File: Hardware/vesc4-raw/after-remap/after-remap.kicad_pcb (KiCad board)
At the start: 4 copper layers, 40.3 x 65 mm, 129 parts, among them K1 SERVO, P1 HALL/Encoder, P101 CANBUS, P2 SWD, P3 PWR_COMM, P4 IN+, P5 IN-, P6 MOTOR1, P7 MOTOR2, P9 MOTOR3, Q1 IPT007N06NATMA1, Q2 IPT007N06NATMA1, Q3 IPT007N06NATMA1, Q4 IPT007N06NATMA1, Q5 IPT007N06NATMA1, Q6 IPT007N06NATMA1, U1 STM32F40X_LQFP64, U2 TC2117, U3 DRV8302, U401 SN65HVD232, X2 8MHz 10ppm

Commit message: pindahin d6
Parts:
- moved D6 25.8 mm to (78.4, 135.5), turned to 90 degrees
- moved C2 0.66 mm to (83.7, 127.1)
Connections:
- net Net-(U4-D+) renamed /D+
- net Net-(U4-D-) renamed /D-
- U4 pad 1: Net-(USB1-VCC) -> Net-(D6-A)
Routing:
- net /D+: track 4.28 -> 6.64 mm
- net /D-: track 3.97 -> 6.16 mm
- net /MCU/AN_IN: track 28.9 -> 27.4 mm

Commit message: usb kelar trace
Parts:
- D4: moved to B.Cu
- moved D4 14.3 mm to (74.0, 120.7), turned to 180 degrees
- moved 1PIN 1.90 mm to (79.6, 142.0)
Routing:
- net GND: track 387.3 -> 395.4 mm
- net Net-(D6-A): track 0.00 -> 5.66 mm
- net +5V: track 115.3 -> 119.3 mm

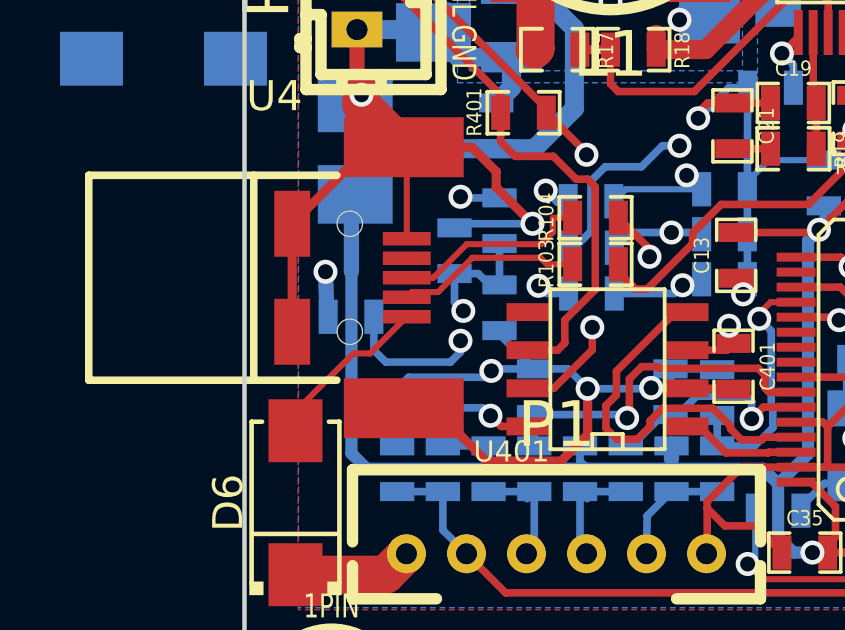
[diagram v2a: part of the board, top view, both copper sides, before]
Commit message: hapus r6 0r sama via
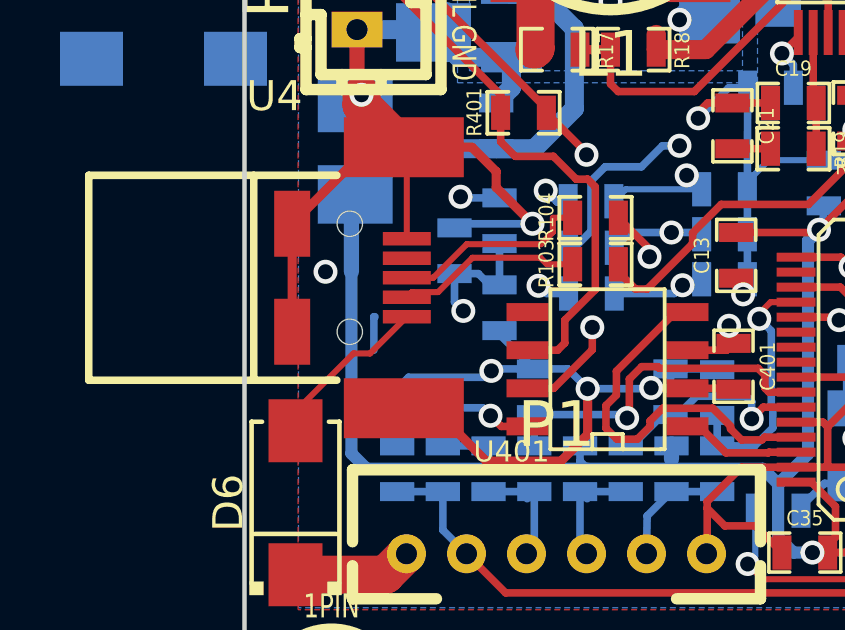
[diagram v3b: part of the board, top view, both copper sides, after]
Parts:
- removed R6: 0R, CRF1:SMD-0603_r
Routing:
- net Net-(USB1-VCC): track 4.72 -> 1.15 mm, vias 1 -> 0
- net +5V: track 119.3 -> 117.8 mm
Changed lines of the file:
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@@
 	(footprint "CRF1:SMD-0603_r"
 		(layer "B.Cu")
-		(at 80.25 129.3 180)
-		(property "Reference" "R6"
-			(at 1.635 -0.024 90)
-			(layer "B.SilkS")
-			(effects
-				(font
-					(size 0.50038 0.4572)
-					(thickness 0.1143)
-				)
-				(justify mirror)
-			)
-		)
-		(property "Value" "0R"
-			(at -1.69926 0 90)
-			(layer "B.SilkS")
-			(hide yes)
-			(effects
-				(font
-					(size 0.508 0.4572)
-					(thickness 0.1143)
-				)
-				(justify mirror)
-			)
-		)
-		(property "Datasheet" ""
-			(at 0 0 0)
-			(layer "B.Fab")
-			(hide yes)
-			(effects
-				(font
-					(size 1.27 1.27)
-					(thickness 0.15)
-				)
-				(justify mirror)
-			)
-		)
-		(property "Description" ""
-			(at 0 0 0)
-			(layer "B.Fab")
-			(hide yes)
-			(effects
-				(font
-					(size 1.27 1.27)
-					(thickness 0.15)
-				)
-				(justify mirror)
-			)
-		)
-		(property ki_fp_filters "R? SM0603 SM0805 R?-* SM1206")
-		(sheetname "/")
-		(sheetfile "after-remap.kicad_sch")
-		(attr smd)
-		(fp_line
-			(start 1.2065 0.6985)
-			(end 1.2065 -0.6985)
-			(stroke
-				(width 0.127)
-				(type solid)
-			)
-			(layer "B.SilkS")
-		)
-		(fp_line
-			(start 1.2065 0.6985)
-			(end 0.50038 0.6985)
-			(stroke
-				(width 0.127)
-				(type solid)
-			)
-			(layer "B.SilkS")
-		)
-		(fp_line
-			(start 1.2065 -0.6985)
-			(end 0.50038 -0.6985)
-			(stroke
-				(width 0.127)
-				(type solid)
-			)
-			(layer "B.SilkS")
-		)
-		(fp_line
-			(start -0.50038 0.6985)
-			(end -1.2065 0.6985)
-			(stroke
-				(width 0.127)
-				(type solid)
-			)
-			(layer "B.SilkS")
-		)
-		(fp_line
-			(start -1.2065 0.6985)
-			(end -1.2065 -0.6985)
-			(stroke
-				(width 0.127)
-				(type solid)
-			)
-			(layer "B.SilkS")
-		)
-		(fp_line
-			(start -1.2065 -0.6985)
-			(end -0.50038 -0.6985)
-			(stroke
-				(width 0.127)
-				(type solid)
-			)
-			(layer "B.SilkS")
-		)
-		(pad "1" smd rect
-			(at -0.762 0 180)
-			(size 0.635 1.143)
-			(layers "B.Cu" "B.Mask" "B.Paste")
-			(net 114 "Net-(USB1-VCC)")
-			(pintype "passive")
-		)
-		(pad "2" smd rect
-			(at 0.762 0 180)
-			(size 0.635 1.143)
-			(layers "B.Cu" "B.Mask" "B.Paste")
-			(net 1 "+5V")
-			(pintype "passive")
-		)
-		(embedded_fonts no)
-		(model "smd\\resistors\\R0603.wrl"
-			(offset
-				(xyz 0 0 0.02540000082)
-			)
-			(scale
-				(xyz 0.5 0.5 0.5)
-			)
-			(rotate
-				(xyz 0 0 0)
-			)
-		)
-	)
-	(footprint "CRF1:SMD-0603_r"
-		(layer "B.Cu")
 		(at 83.312 134.366 90)
 		(property "Reference" "R7"
@@
 	)
 	(segment
-		(start 79.45 129.262)
-		(end 79.4 127.8)
-		(width 0.508)
-		(layer "B.Cu")
-		(net 1)
-	)
-	(segment
 		(start 83.698 116.078)
 		(end 83 116.776)
@@
 	)
 	(segment
-		(start 79.488 129.3)
-		(end 79.45 129.262)
-		(width 0.508)
-		(layer "B.Cu")
-		(net 1)
-	)
-	(segment
 		(start 108.63326 133.096)
 		(end 108.63326 133.27126)
@@
 		(net 96)
 	)
-	(via
-		(at 83.9 130.1)
-		(size 0.8)
-		(drill 0.5)
-		(layers "F.Cu" "B.Cu")
-		(net 114)
-	)
 	(segment
 		(start 81.05 129.3)
@@
 	)
 	(segment
-		(start 83.9 130.476)
-		(end 83.566 130.81)
-		(width 0.254)
-		(layer "B.Cu")
-		(net 114)
-	)
-	(segment
-		(start 83.566 130.81)
-		(end 81.407 130.81)
-		(width 0.254)
-		(layer "B.Cu")
-		(net 114)
-	)
-	(segment
-		(start 81.407 130.81)
-		(end 81.012 130.415)
-		(width 0.254)
-		(layer "B.Cu")
-		(net 114)
-	)
-	(segment
 		(start 81.012 130.415)
 		(end 81.012 129.3)
 		(width 0.254)
 		(layer "B.Cu")
-		(net 114)
-	)
-	(segment
-		(start 83.9 130.1)
-		(end 83.9 130.476)
-		(width 0.254)
-		(layer "B.Cu")

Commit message: sebelum pasang d4
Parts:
- moved D4 2.04 mm to (72.0, 120.3)
- moved C25 0.98 mm to (79.5, 124.1), turned to 0 degrees
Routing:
- net GND: track 395.4 -> 399.5 mm
- net +5V: track 117.8 -> 115.8 mm, vias 4 -> 3
- net VCC: track 185.3 -> 186.6 mm

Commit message: habis pasang d4
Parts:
- removed the D4 at (87.0, 113.0)
- moved D4 16.7 mm to (87.0, 113.0)
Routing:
- net GND: track 399.5 -> 396.9 mm
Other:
- board text added: "SEM"

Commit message: cp
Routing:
- net /Power MOSFETS/Q2-g: track 18.6 -> 17.3 mm
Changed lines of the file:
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@@
-	)
-	(segment
-		(start 104.394 95.377)
-		(end 104.871 94.9)
-		(width 0.2032)
-		(layer "B.Cu")
-		(net 86)
 	)
 	(segment
@@
 	)
 	(segment
-		(start 105.5939 94.9029)
-		(end 114.4029 94.9029)
+		(start 105.7419 96.7249)
+		(end 114.6902 96.7249)
 		(width 0.2032)
 		(layer "B.Cu")
@@
 	)
 	(segment
-		(start 104.871 94.9)
-		(end 105.5939 94.9)
+		(start 104.394 95.377)
+		(end 105.7419 96.7249)
+		(width 0.2032)
+		(layer "B.Cu")
+		(net 86)
+	)
+	(segment
+		(start 114.6902 96.7249)
+		(end 114.8 96.8347)
+		(width 0.2032)
+		(layer "B.Cu")
+		(net 86)
+	)
+	(segment
+		(start 114.8 96.8347)
+		(end 114.8 98.6)
 		(width 0.2032)
 		(layer "B.Cu")
@@
 		(width 0.2032)
 		(layer "B.Cu")
-		(net 86)
-	)
-	(segment
-		(start 105.5939 94.9)
-		(end 105.5939 94.9029)
-		(width 0.2032)
-		(layer "B.Cu")
-		(net 86)
-	)
-	(segment
-		(start 114.8 95.3)
-		(end 114.8 98.6)
-		(width 0.2032)
-		(layer "B.Cu")
-		(net 86)
-	)
-	(segment
-		(start 114.4029 94.9029)
-		(end 114.8 95.3)
-		(width 0.2032)
-		(layer "B.Cu")

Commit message: checkpoint
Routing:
- net Net-(USB1-VCC): track 1.15 -> 0.00 mm
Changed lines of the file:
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@@
 		(tenting front back)
 		(pcbplotparams
-			(layerselection 0x00000000_00000000_00000000_0200a0ff)
+			(layerselection 0x00000000_00000000_55555555_5755f5ff)
 			(plot_on_all_layers_selection 0x00000000_00000000_00000000_00000000)
 			(disableapertmacros no)
@@
 	(net 112 "unconnected-(U3-PWRGD-Pad4)")
 	(net 113 "unconnected-(U401-Vref-Pad5)")
-	(net 114 "Net-(USB1-VCC)")
-	(net 115 "Net-(D6-A)")
-	(net 116 "unconnected-(U4-ID-Pad4)")
+	(net 114 "Net-(D6-A)")
+	(net 115 "unconnected-(U4-ID-Pad4)")
 	(footprint "VESC4-legacy:1pin"
 		(layer "F.Cu")
@@
 			(size 1.6 0.45)
 			(layers "F.Cu" "F.Mask" "F.Paste")
-			(net 115 "Net-(D6-A)")
+			(net 114 "Net-(D6-A)")
 			(pinfunction "VCC")
 			(pintype "input")
@@
 			(size 1.6 0.45)
 			(layers "F.Cu" "F.Mask" "F.Paste")
-			(net 116 "unconnected-(U4-ID-Pad4)")
+			(net 115 "unconnected-(U4-ID-Pad4)")
 			(pinfunction "ID")
 			(pintype "input+no_connect")
@@
 			(size 2.1 1.8)
 			(layers "F.Cu" "F.Mask" "F.Paste")
-			(net 115 "Net-(D6-A)")
+			(net 114 "Net-(D6-A)")
 			(pinfunction "A")
 			(pintype "unspecified")
@@
 	)
 	(segment
-		(start 81.05 129.3)
-		(end 81.012 129.3)
-		(width 0.254)
-		(layer "B.Cu")
-		(net 114)
-	)
-	(segment
-		(start 81.012 130.415)
-		(end 81.012 129.3)
-		(width 0.254)
-		(layer "B.Cu")
-		(net 114)
-	)
-	(segment
 		(start 80.886036 130.523964)
 		(end 80.330836 130.523964)
 		(width 0.2032)
 		(layer "F.Cu")
-		(net 115)
+		(net 114)
 	)
 	(segment
@@
 		(width 0.2032)
 		(layer "F.Cu")
-		(net 115)
+		(net 114)
 	)
 	(segment
@@
 		(width 0.2032)
 		(layer "F.Cu")
-		(net 115)
+		(net 114)
 	)
 	(segment
@@
 		(width 0.2032)
 		(layer "F.Cu")
-		(net 115)
+		(net 114)
 	)
 	(zone

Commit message: cp
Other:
- board size 40.3 x 65 mm -> 41.2 x 65 mm
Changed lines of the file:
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@@
 	(gr_line
 		(start 111 145)
-		(end 117 145)
+		(end 117.8681 145)
 		(stroke
 			(width 0.15)
@@
 	)
 	(gr_line
-		(start 117 80)
-		(end 117 145)
+		(start 117.8681 80)
+		(end 117.8681 145)
 		(stroke
 			(width 0.15)
@@
 	)
 	(gr_line
-		(start 117 80)
+		(start 117.8681 80)
 		(end 76.7 80)
 		(stroke
